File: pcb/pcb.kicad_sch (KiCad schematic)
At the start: 57 parts, among them J1 USB_C_Receptacle_USB2.0_16P, J2 Conn_01x02, K1 SW_Push, K10 SW_Push, K11 SW_Push, K12 SW_Push, K13 SW_Push, K14 SW_Push, K15 SW_Push, K16 SW_Push, K17 SW_Push, K18 SW_Push, K19 SW_Push, K2 SW_Push, K20 SW_Push, K21 SW_Push, K3 SW_Push, K4 SW_Push, K5 SW_Push, K6 SW_Push, K7 SW_Push, K8 SW_Push, K9 SW_Push, U1 SRV05-4, U2 ProMicro, U3 SRV05-4

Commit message: cirrus40, second manufactured version
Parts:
- removed D19, D20, D22: DIODE, footprints:Diode-dual, symbol cirrus40:DIODE
- removed K19, K20, K21: SW_Push, footprints:SW_MX_HotSwap_Reversible, symbol cirrus40:SW_Push
- added C1, C3: 470nF, Capacitor_SMD:C_0805_2012Metric_Pad1.18x1.45mm_HandSolder, symbol cirrus40:C_Small
- added D12, D21: DIODE, footprints:Diode-dual, symbol cirrus40:DIODE
- added R1, R2, R5, R6: 10kOhm, Resistor_SMD:R_0805_2012Metric_Pad1.20x1.40mm_HandSolder, symbol Device:R
- added R3, R4, R7, R8: 8kOhm, Resistor_SMD:R_0805_2012Metric_Pad1.20x1.40mm_HandSolder, symbol Device:R
- C2: renamed from C1; value 50V/100nF axial -> 470nF; footprint footprints:RESISTOR_Reversible -> Capacitor_SMD:C_0805_2012Metric_Pad1.18x1.45mm_HandSolder
- C4: renamed from C2; value 50V/100nF axial -> 470nF; footprint footprints:RESISTOR_Reversible -> Capacitor_SMD:C_0805_2012Metric_Pad1.18x1.45mm_HandSolder
- FB1: renamed from FB2; footprint footprints:C_0603_1608Metric_Pad1.08x0.95mm_HandSolder -> Capacitor_SMD:C_0805_2012Metric_Pad1.18x1.45mm_HandSolder
- FB2: renamed from FB3; footprint footprints:C_0603_1608Metric_Pad1.08x0.95mm_HandSolder -> Capacitor_SMD:C_0805_2012Metric_Pad1.18x1.45mm_HandSolder
- FB3: renamed from FB4; footprint footprints:C_0603_1608Metric_Pad1.08x0.95mm_HandSolder -> Capacitor_SMD:C_0805_2012Metric_Pad1.18x1.45mm_HandSolder
- FB4: renamed from FB1; footprint footprints:C_0603_1608Metric_Pad1.08x0.95mm_HandSolder -> Capacitor_SMD:C_0805_2012Metric_Pad1.18x1.45mm_HandSolder
- renumbered D13 to D1, D9 to D10, D18 to D11, D4 to D13, D5 to D14, D6 to D15, D17 to D16, D1 to D17, D2 to D18, D3 to D19, D14 to D2, D16 to D20, D15 to D3, D10 to D4, D11 to D5, D12 to D6, D21 to D7, D7 to D8, D8 to D9, K13 to K1, K18 to K10, K4 to K11, K5 to K12, K6 to K13, K17 to K14, K1 to K15, K2 to K16, K3 to K17, K16 to K18, K14 to K2, K15 to K3, K10 to K4, K11 to K5, K12 to K6, U3 to U1, U1 to U2, U2 to U3
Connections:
- net COL5 is gone; now on net COL4: U3.20 (GP20)
- net COL0: now also U3.28 (GP28); no longer U3.29 (GP29)
- net COL1: now also U3.27 (GP27); no longer U3.28 (GP28)
- net COL2: now also U3.26 (GP26); no longer U3.27 (GP27)
- net COL3: now also U3.22 (GP22); no longer U3.26 (GP26)
- net COL4: no longer U3.22 (GP22)
- net ENCA: now also D12.1 (K), R1.2, R2.2, R3.1, R4.1; no longer C2.1, U3.6 (GP6)
- net ENCB: now also D21.1 (K), R5.2, R6.2, R7.1, R8.1; no longer C4.2, U3.7 (GP7)
- net GND: now also C4.2, C1.2, C3.2; no longer C4.1
- net ROW0: now also U3.3 (GP3); no longer U3.2 (GP2)
- net ROW1: now also U3.4 (GP4); no longer U3.3 (GP3)
- net ROW2: now also U3.5 (GP5); no longer U3.4 (GP4)
- net ROW3: now also U3.6 (GP6); no longer U3.5 (GP5)
- net VCC: now also R1.1, R2.1, R5.1, R6.1
- net ENCA_DB: now reaches U3.8 (GP8)
- net ENCA_DB: now also C2.1, C1.1, D12.2 (A), R3.2, R4.2
- net ENCB_DB: now reaches U3.9 (GP9)
- net ENCB_DB: now also C4.1, C3.1, D21.2 (A), R7.2, R8.2
- no-connect marks 25 -> 26
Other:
- note added: "* Move ENCA ENCB to pins 8 and 9. * Route 2 data pins via USBC. For max flexibility, use UART pins 0 and 1. * Make debouncing R and C reversible (two symbols, front/back)."
- moved on the sheet: C2, C4, D7, ENC1, J2, S1, S2

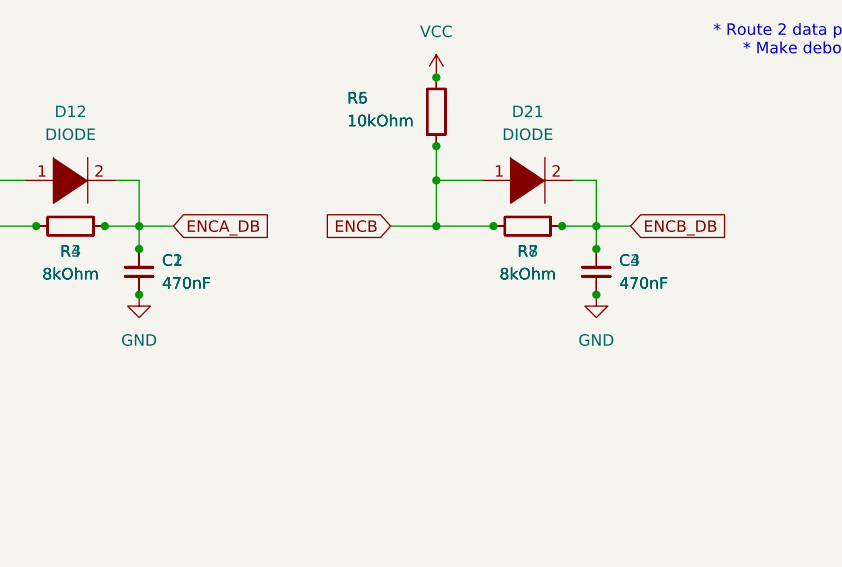
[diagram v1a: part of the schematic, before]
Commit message: add cap/resistor labels and github link
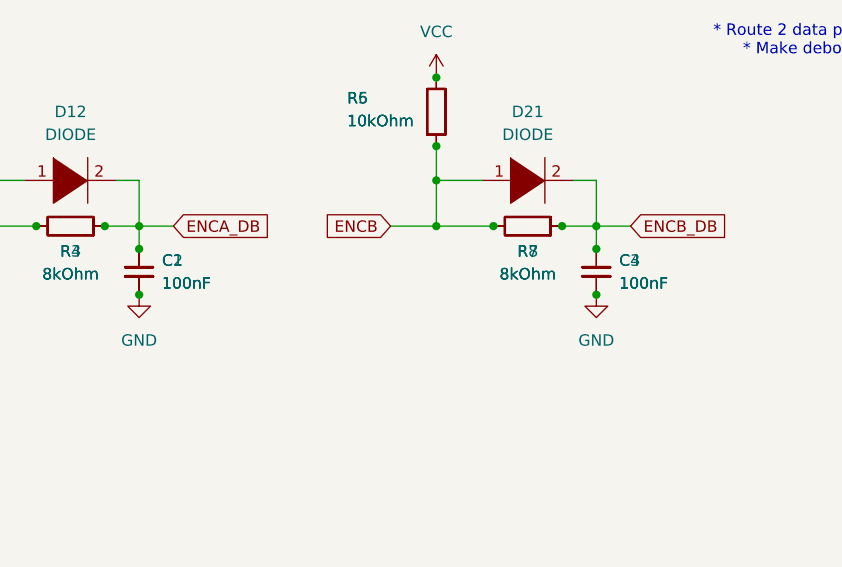
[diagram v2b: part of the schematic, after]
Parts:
- C1, C2, C3, C4: value 470nF -> 100nF
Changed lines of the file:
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@@
 			)
 		)
-		(property "Value" "470nF"
+		(property "Value" "100nF"
 			(at 151.13 133.3562 0)
 			(effects
@@
 			)
 		)
-		(property "Value" "470nF"
+		(property "Value" "100nF"
 			(at 151.13 133.3562 0)
 			(effects
@@
 			)
 		)
-		(property "Value" "470nF"
+		(property "Value" "100nF"
 			(at 201.93 133.3562 0)
 			(effects
@@
 			)
 		)
-		(property "Value" "470nF"
+		(property "Value" "100nF"
 			(at 201.93 133.3562 0)
 			(effects
